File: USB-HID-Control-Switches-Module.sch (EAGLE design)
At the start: 3 parts, among them M1 PRO_MICRO_SMD

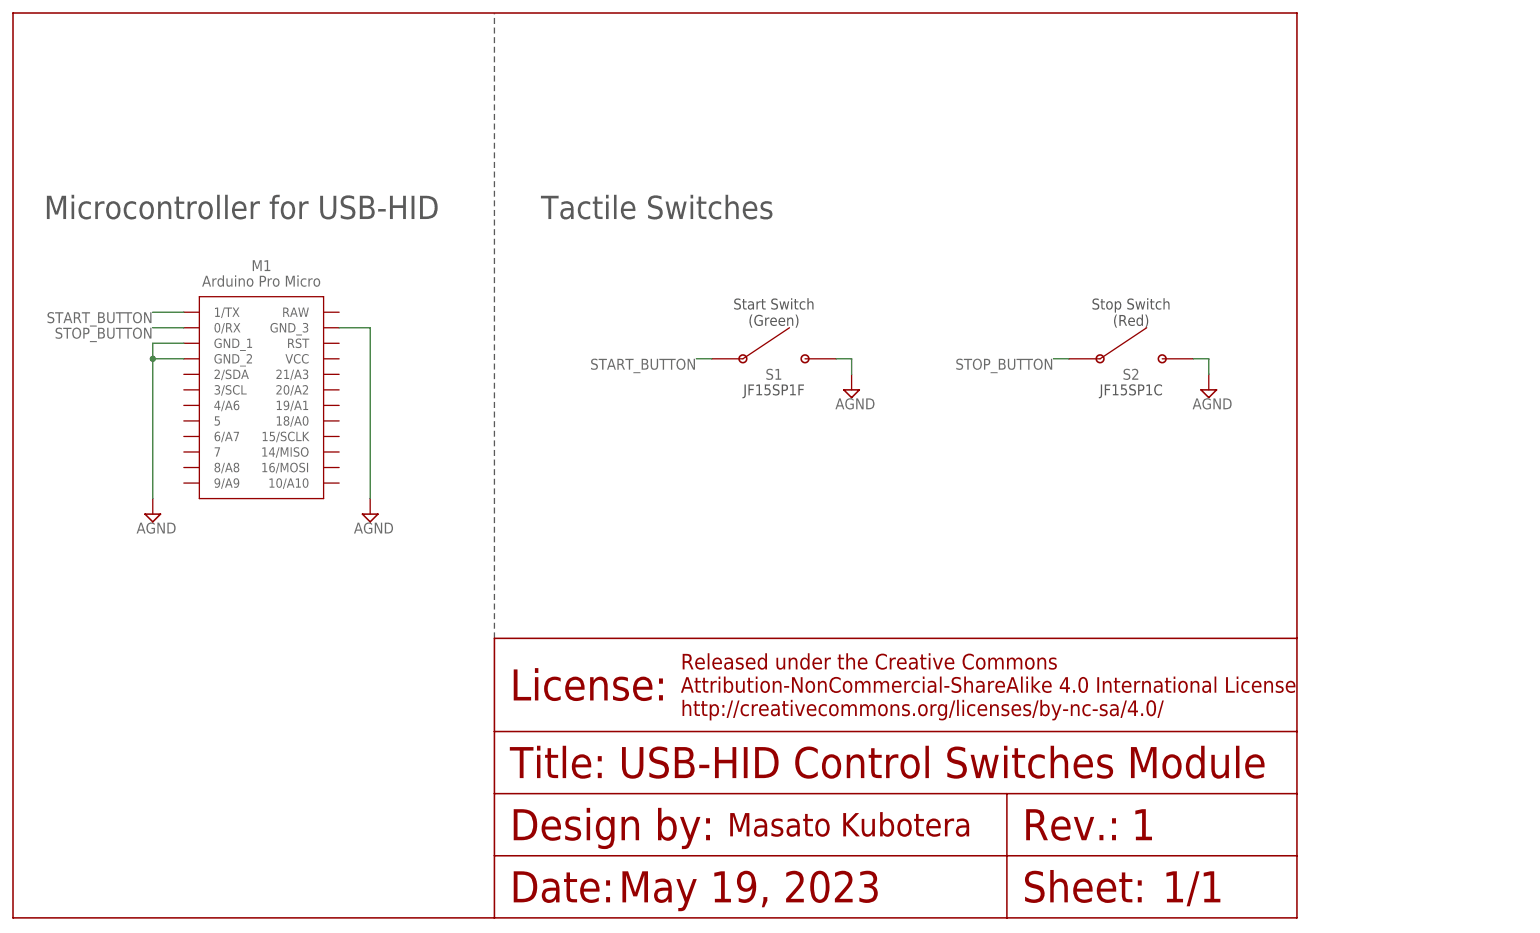
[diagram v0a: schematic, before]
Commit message: Additional LED for status check
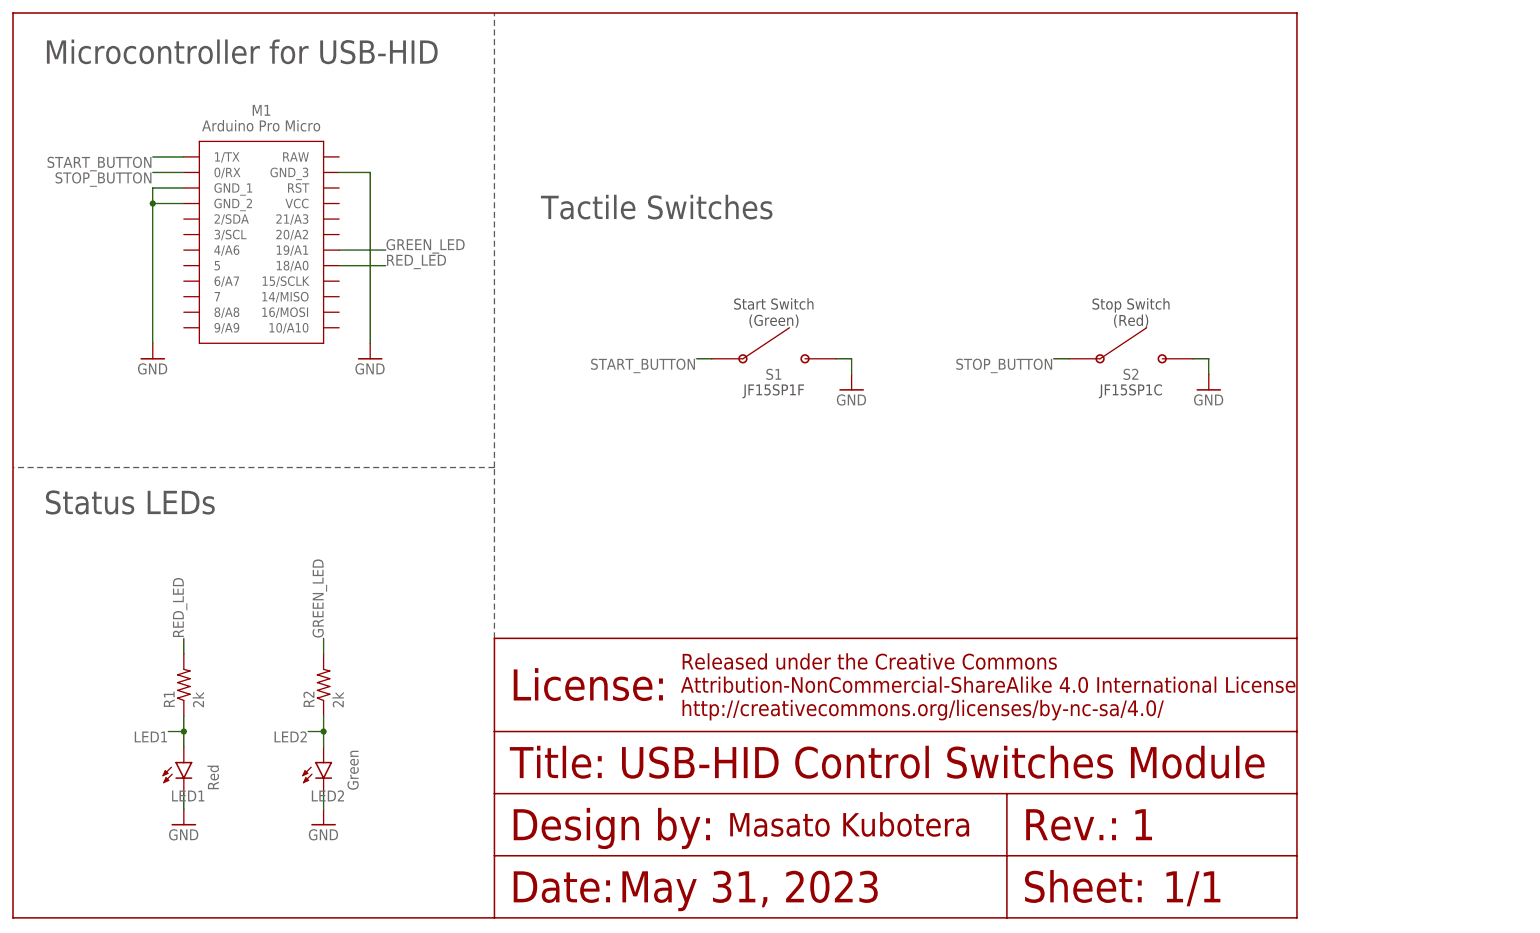
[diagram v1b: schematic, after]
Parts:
- added LED1: Red, led:LEDSML0603
- added LED2: Green, led:LEDSML0603
- added R1, R2: 2k, rcl:R-US_R0603
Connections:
- removed net AGND: M1.GND_1, M1.GND_2, M1.GND_3, S1.P$2, S2.P$2
- new net GND: LED1.C, LED2.C, M1.GND_1, M1.GND_2, M1.GND_3, S1.P$2, S2.P$2
- new net GREEN_LED: M1.19/A1, R2.2
- new net LED1: LED1.A, R1.1
- new net LED2: LED2.A, R2.1
- new net RED_LED: M1.18/A0, R1.2
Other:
- note added: "May 31, 2023"
- note added: "Status LEDs"
- note removed: "May 19, 2023"
- moved on the sheet: M1
